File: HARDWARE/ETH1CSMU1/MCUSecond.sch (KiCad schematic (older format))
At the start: 30 parts, among them J201 Conn_02x05, U201 24LC08, U202 STM32F746ZGTx, X201 ABMM2-8.000MHZ

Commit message: check in
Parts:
- X201: footprint (none) -> SMD:ABMM2
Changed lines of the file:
@@
 F 0 "X201" V 1700 3850 60  0000 L CNN
 F 1 "ABMM2-8.000MHZ" V 1800 3550 60  0000 L CNN
-F 2 "" H 2000 3500 60  0001 C CNN
+F 2 "SMD:ABMM2" H 2000 3500 60  0001 C CNN
 F 3 "" H 2000 3500 60  0000 C CNN
 	1    2000 3500

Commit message: Check in
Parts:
- C204, C208: footprint (none) -> SMD:C_0603_Symbol6
- C205, C206: footprint (none) -> SMD:C_0603_Symbol7
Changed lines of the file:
@@
 F 0 "C204" H 3065 2796 50  0000 L CNN
 F 1 "1u" H 3065 2705 50  0000 L CNN
-F 2 "" H 2988 2600 50  0001 C CNN
+F 2 "SMD:C_0603_Symbol6" H 2988 2600 50  0001 C CNN
 F 3 "~" H 2950 2750 50  0001 C CNN
 	1    2950 2750
@@
 F 0 "C205" H 3515 2796 50  0000 L CNN
 F 1 "2u2" H 3515 2705 50  0000 L CNN
-F 2 "" H 3438 2600 50  0001 C CNN
+F 2 "SMD:C_0603_Symbol7" H 3438 2600 50  0001 C CNN
 F 3 "~" H 3400 2750 50  0001 C CNN
 	1    3400 2750
@@
 F 0 "C206" H 3965 2796 50  0000 L CNN
 F 1 "2u2" H 3965 2705 50  0000 L CNN
-F 2 "" H 3888 2600 50  0001 C CNN
+F 2 "SMD:C_0603_Symbol7" H 3888 2600 50  0001 C CNN
 F 3 "~" H 3850 2750 50  0001 C CNN
 	1    3850 2750
@@
 F 0 "C208" H 4415 10696 50  0000 L CNN
 F 1 "1u" H 4415 10605 50  0000 L CNN
-F 2 "" H 4338 10500 50  0001 C CNN
+F 2 "SMD:C_0603_Symbol6" H 4338 10500 50  0001 C CNN
 F 3 "~" H 4300 10650 50  0001 C CNN
 	1    4300 10650

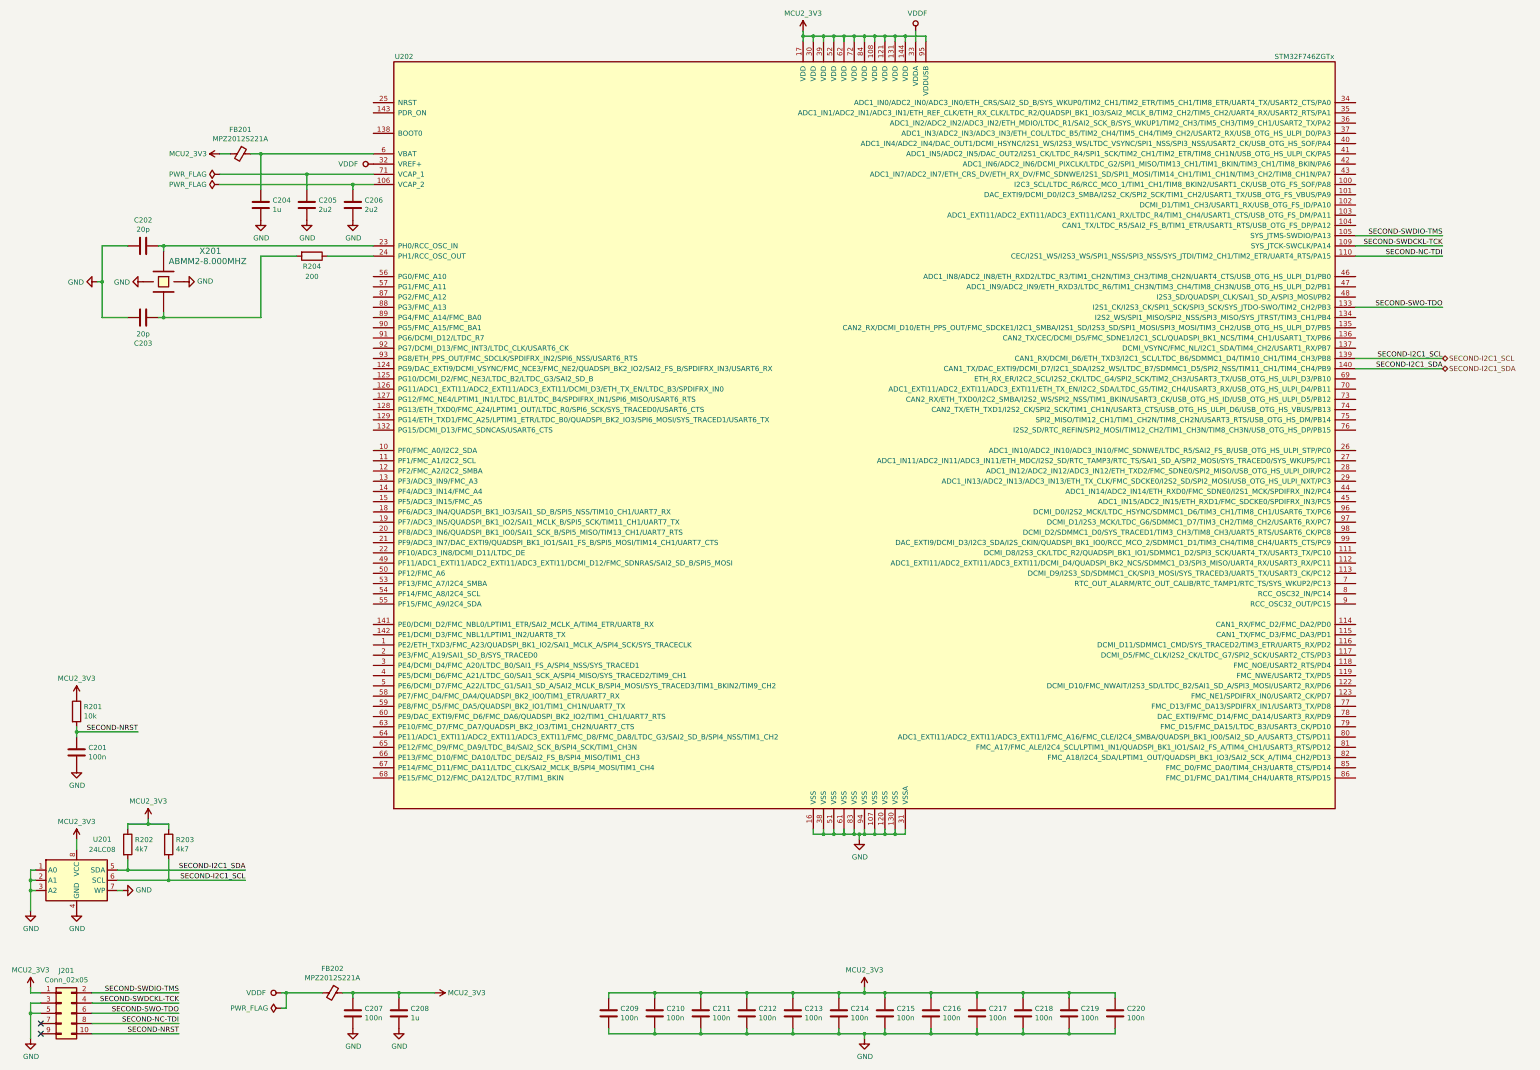
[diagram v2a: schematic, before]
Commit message: Added test circuits, bug fix.
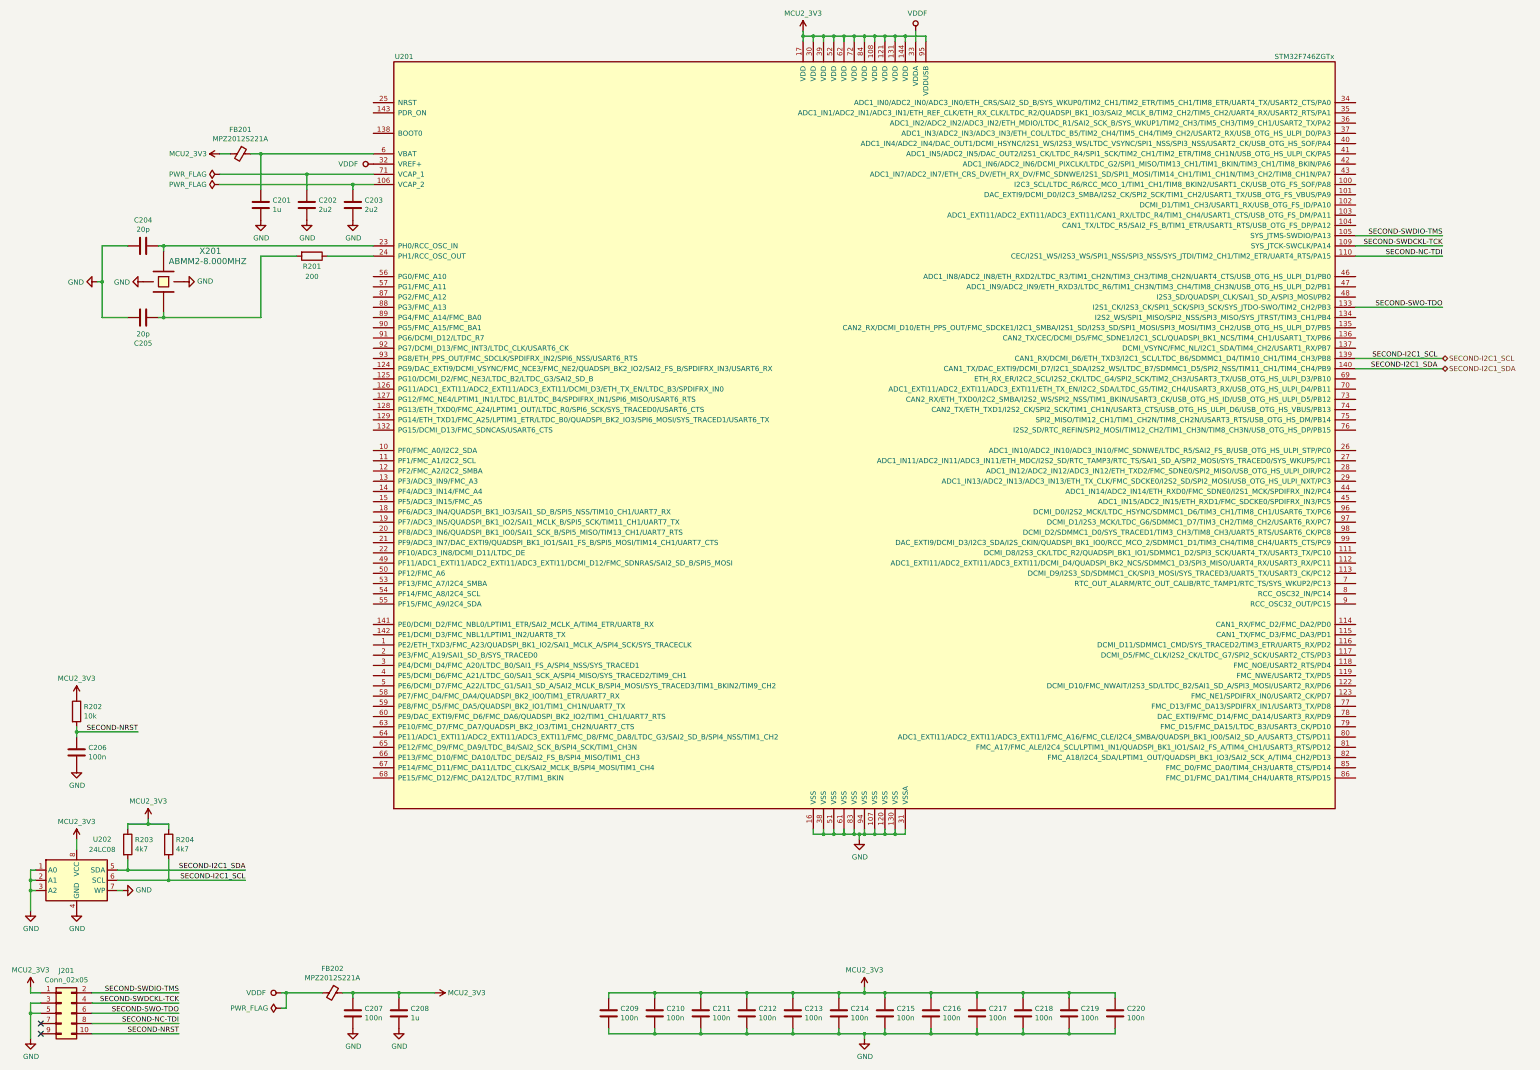
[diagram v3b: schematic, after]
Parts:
- renumbered C204 to C201, C205 to C202, C206 to C203, C202 to C204, C203 to C205, C201 to C206, R204 to R201, R201 to R202, R202 to R203, R203 to R204, U202 to U201, U201 to U202
